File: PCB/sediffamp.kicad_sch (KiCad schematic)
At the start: 15 parts, among them U13 OPA1622

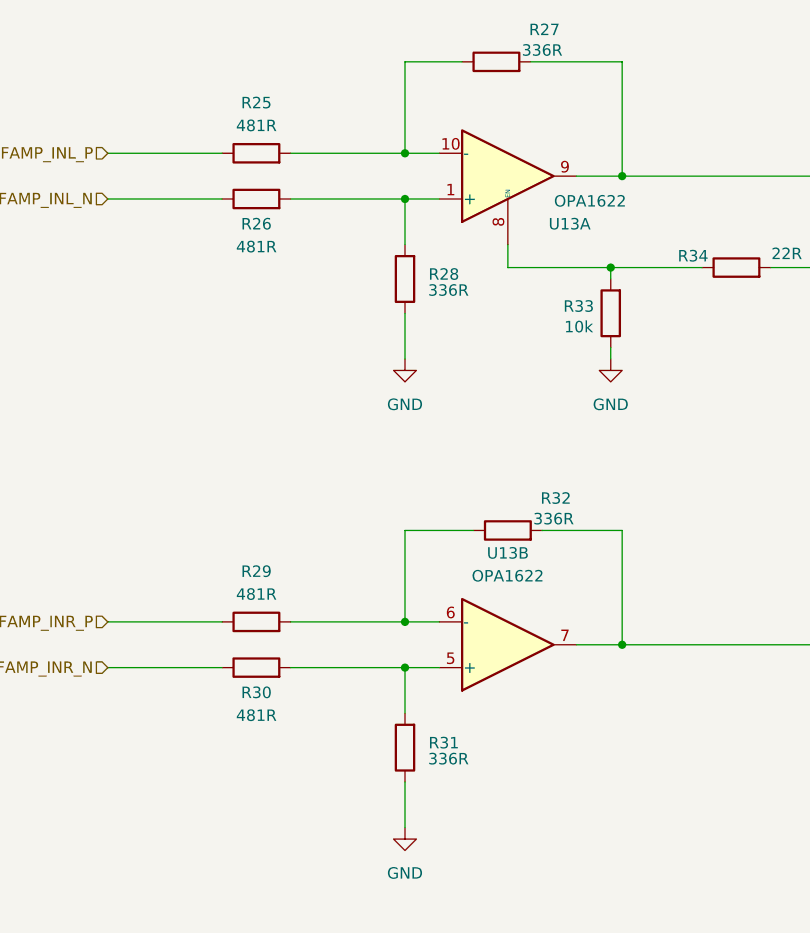
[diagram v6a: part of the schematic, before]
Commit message: Changed resistor values to match JLCPCB + general board revision
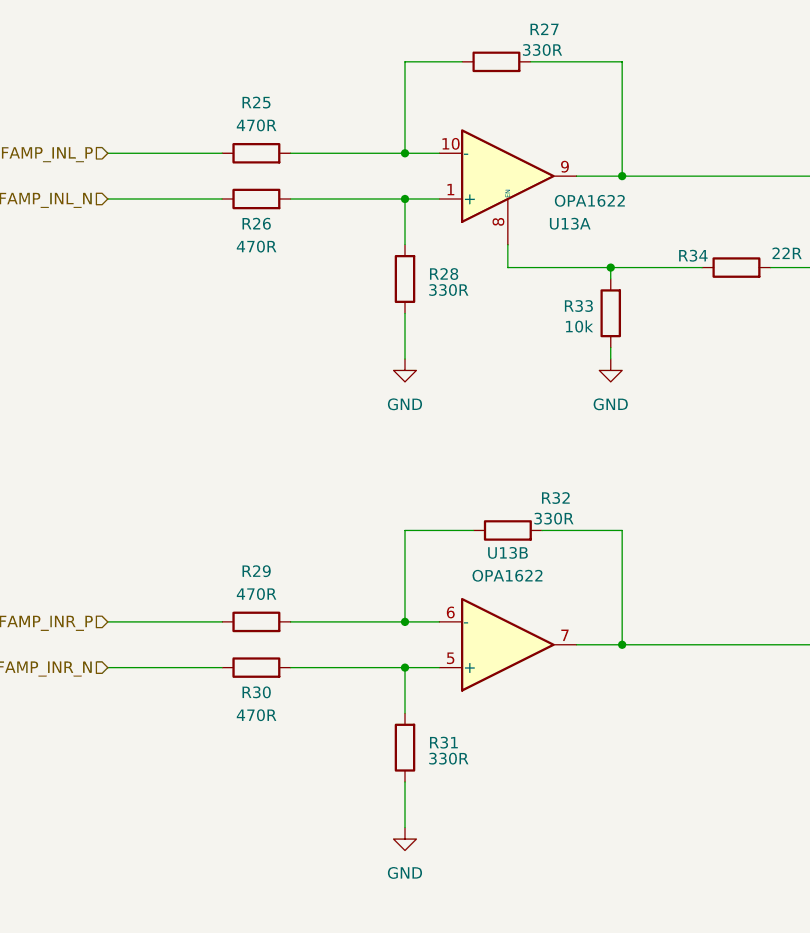
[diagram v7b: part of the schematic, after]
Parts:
- R25, R26, R29, R30: value 481R -> 470R; JLCPCBPn (none) -> C445590
- R27, R28, R31, R32: value 336R -> 330R; JLCPCBPn (none) -> C186314
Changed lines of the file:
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@@
 			)
 		)
-		(property "Value" "481R"
+		(property "Value" "470R"
 			(at 111.76 47.752 90)
 			(effects
@@
 			)
 		)
+		(property "JLCPCBPn" "C445590"
+			(at 111.76 50.8 0)
+			(effects
+				(font
+					(size 1.27 1.27)
+				)
+				(hide yes)
+			)
+		)
 		(pin "1"
 		)
@@
 			)
 		)
-		(property "Value" "481R"
+		(property "Value" "470R"
 			(at 111.76 99.822 90)
 			(effects
@@
 		)
 		(property "Tolerance" "0.1%"
+			(at 111.76 102.87 0)
+			(effects
+				(font
+					(size 1.27 1.27)
+				)
+				(hide yes)
+			)
+		)
+		(property "JLCPCBPn" "C445590"
 			(at 111.76 102.87 0)
 			(effects
@@
 			)
 		)
-		(property "Value" "336R"
+		(property "Value" "330R"
 			(at 133.096 118.11 0)
 			(effects
@@
 			)
 		)
+		(property "JLCPCBPn" "C186314"
+			(at 128.27 116.84 0)
+			(effects
+				(font
+					(size 1.27 1.27)
+				)
+				(hide yes)
+			)
+		)
 		(pin "1"
 		)
@@
 			)
 		)
-		(property "Value" "481R"
+		(property "Value" "470R"
 			(at 111.76 113.284 90)
 			(effects
@@
 		)
 		(property "Tolerance" "0.1%"
+			(at 111.76 107.95 0)
+			(effects
+				(font
+					(size 1.27 1.27)
+				)
+				(hide yes)
+			)
+		)
+		(property "JLCPCBPn" "C445590"
 			(at 111.76 107.95 0)
 			(effects
@@
 			)
 		)
-		(property "Value" "336R"
+		(property "Value" "330R"
 			(at 144.78 91.44 90)
 			(effects
@@
 			)
 		)
+		(property "JLCPCBPn" "C186314"
+			(at 139.7 92.71 0)
+			(effects
+				(font
+					(size 1.27 1.27)
+				)
+				(hide yes)
+			)
+		)
 		(pin "1"
 		)
@@
 			)
 		)
-		(property "Value" "481R"
+		(property "Value" "470R"
 			(at 111.76 61.214 90)
 			(effects
@@
 			)
 		)
+		(property "JLCPCBPn" "C445590"
+			(at 111.76 55.88 0)
+			(effects
+				(font
+					(size 1.27 1.27)
+				)
+				(hide yes)
+			)
+		)
 		(pin "1"
 		)
@@
 			)
 		)
-		(property "Value" "336R"
+		(property "Value" "330R"
 			(at 143.51 39.37 90)
 			(effects
@@
 		)
 		(property "Tolerance" "0.1%"
+			(at 138.43 40.64 0)
+			(effects
+				(font
+					(size 1.27 1.27)
+				)
+				(hide yes)
+			)
+		)
+		(property "JLCPCBPn" "C186314"
 			(at 138.43 40.64 0)
 			(effects
@@
 			)
 		)
-		(property "Value" "336R"
+		(property "Value" "330R"
 			(at 133.096 66.04 0)
 			(effects
@@
 			(at 128.27 64.77 0)
 			(effects
+				(font
+					(size 1.27 1.27)
+				)
+				(hide yes)
+			)
+		)
+		(property "JLCPCBPn" "C186314"
+			(at 128.27 64.77 0)
+			(effects

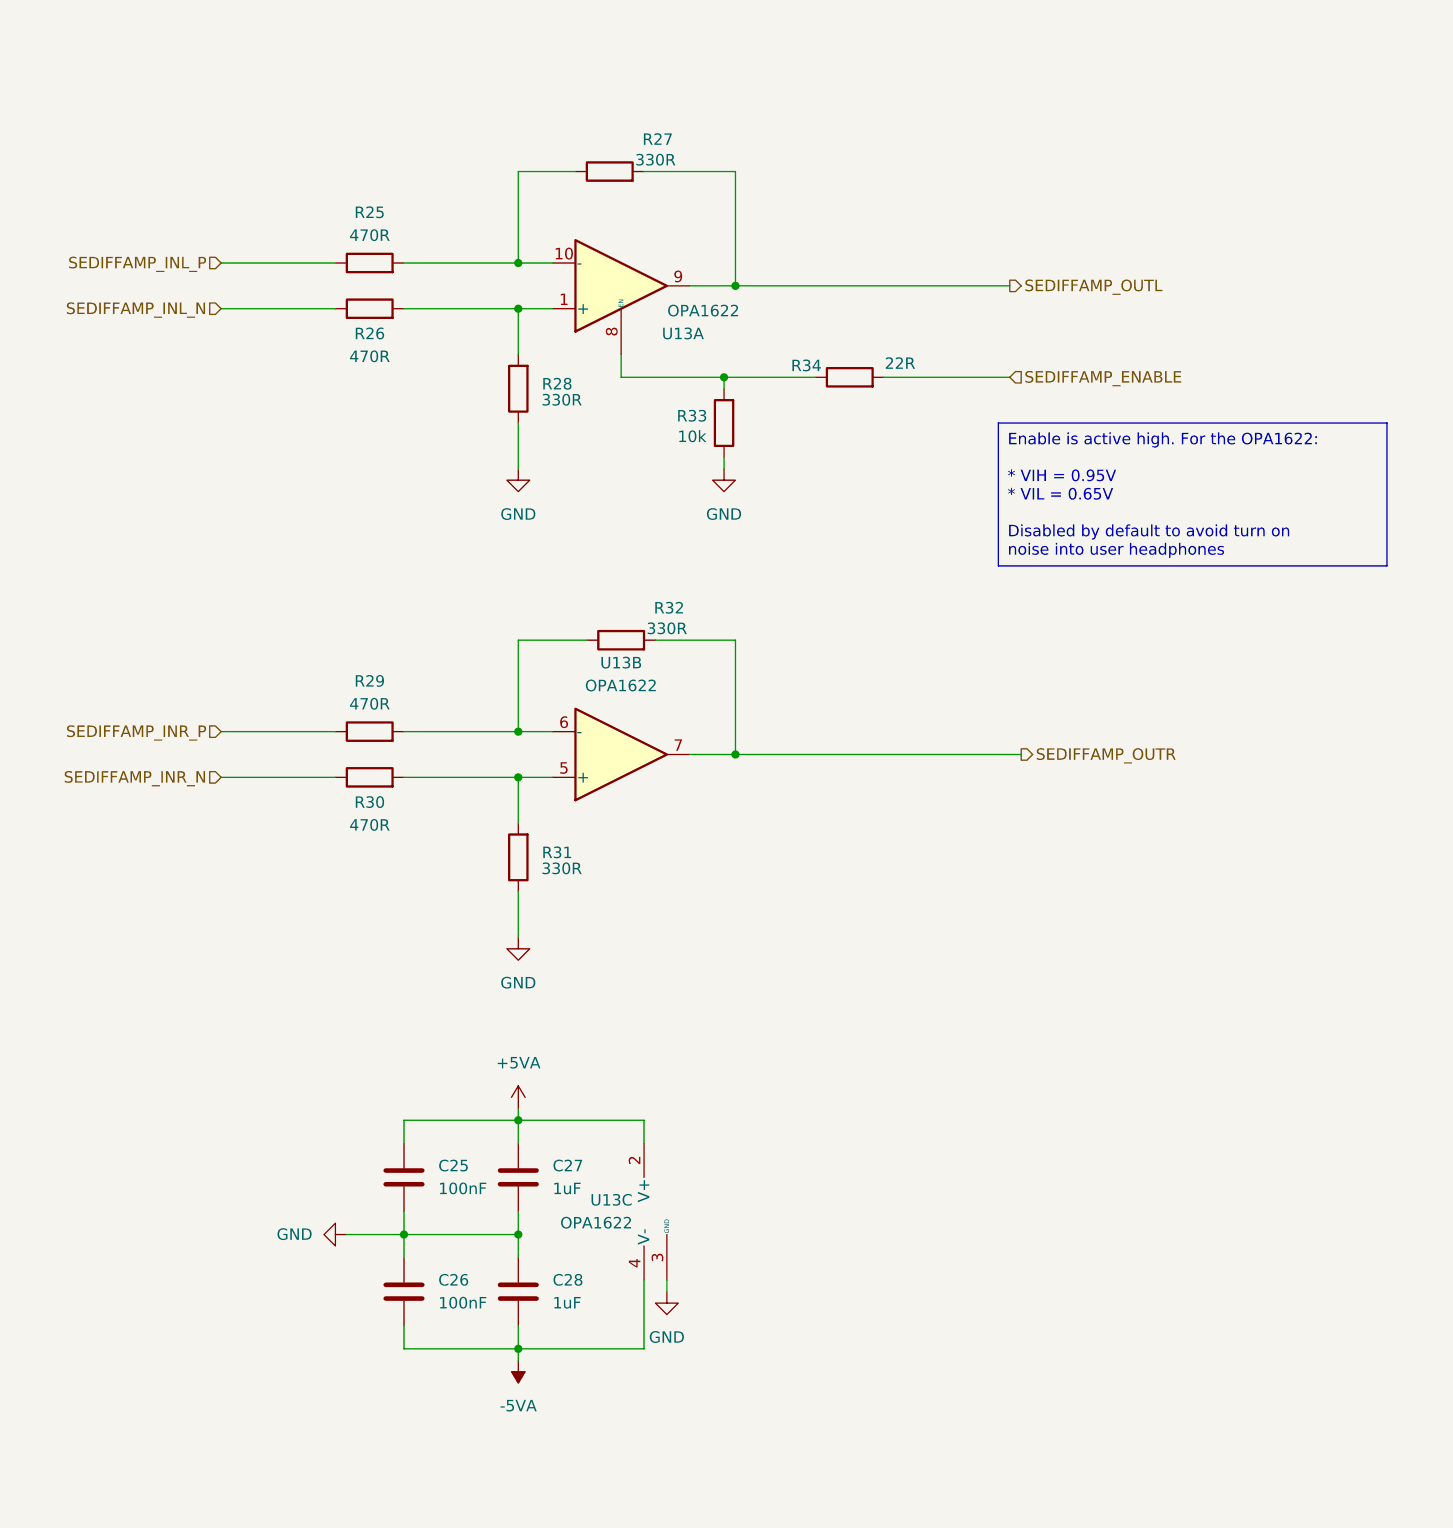
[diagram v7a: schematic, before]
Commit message: Added filter capacitors to OPA1622 circuitry
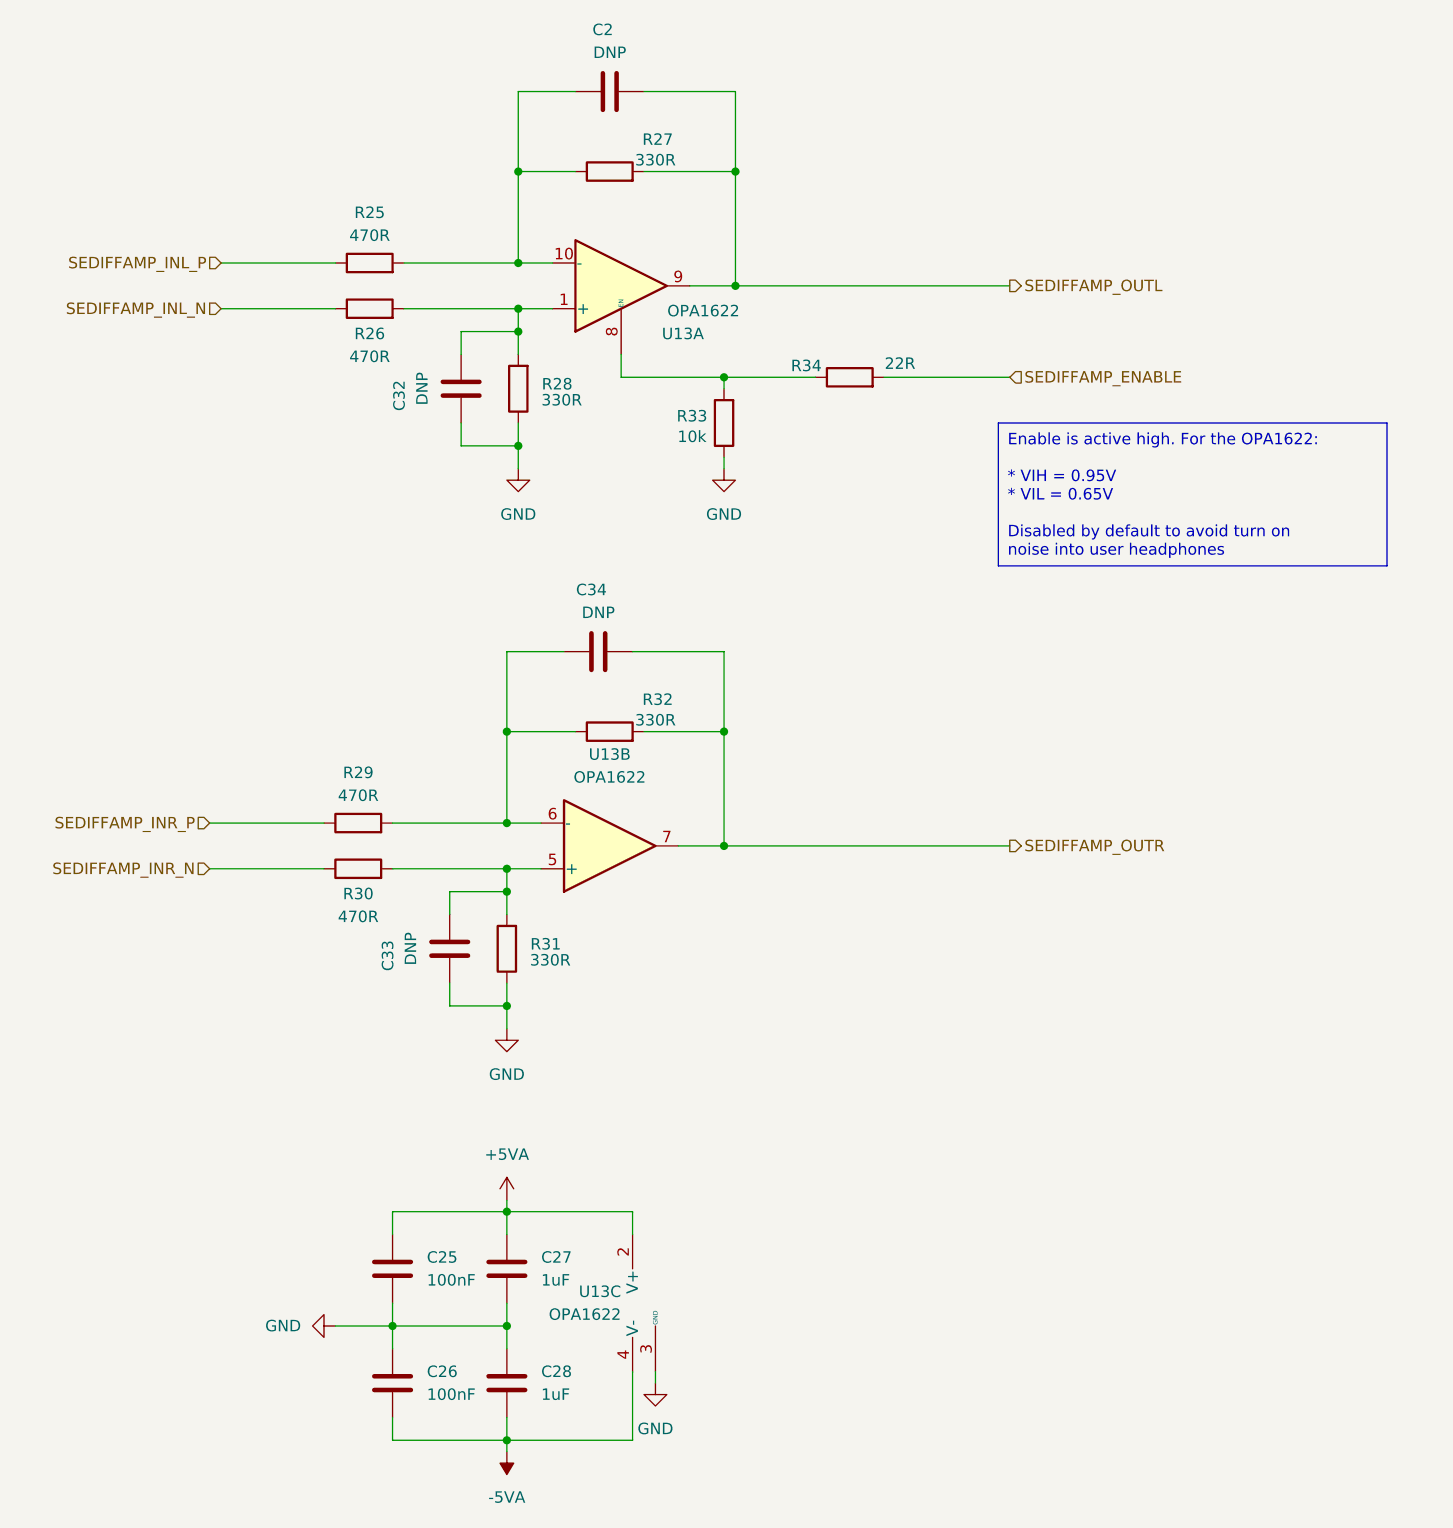
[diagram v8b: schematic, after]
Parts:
- added C2, C32, C33, C34: DNP, Capacitor_SMD:C_0603_1608Metric_Pad1.08x0.95mm_HandSolder, symbol Device:C
- C25, C26: JLCPCBPn C1525 -> (none); LCSC Part # (none) -> C1525
- C27, C28: JLCPCBPn C15849 -> (none); LCSC Part # (none) -> C15849
- R25, R26, R29, R30: JLCPCBPn C445590 -> (none); LCSC Part # (none) -> C445590
- R27, R28, R31, R32: JLCPCBPn C186314 -> (none); LCSC Part # (none) -> C186314
- R33: JLCPCBPn C25744 -> (none); LCSC Part # (none) -> C25744
- R34: JLCPCBPn C25092 -> (none); LCSC Part # (none) -> C25092
- U13: JLCPCBPn C2876559 -> (none); LCSC Part # (none) -> C2876559
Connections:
- net GND: now also C32.1, C33.1
- net SEDIFFAMP_OUTL: now also C2.2
- net SEDIFFAMP_OUTR: now also C34.2
- net at R30.2, R31.2, U13.5 (+): now also C33.2
- net at R29.2, R32.1, U13.6 (-): now also C34.1
- net at R26.2, R28.2, U13.1 (+): now also C32.2
- net at R25.2, R27.1, U13.10 (-): now also C2.1
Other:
- moved on the sheet: C25, C26, C27, C28, R29, R30, R31, R32, U13B, U13C
